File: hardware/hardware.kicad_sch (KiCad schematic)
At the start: 5 parts, among them J1 USB_C_Receptacle_USB2.0_14P, J3 Conn_01x08_Socket, U2 ESP32-S3-WROOM-1

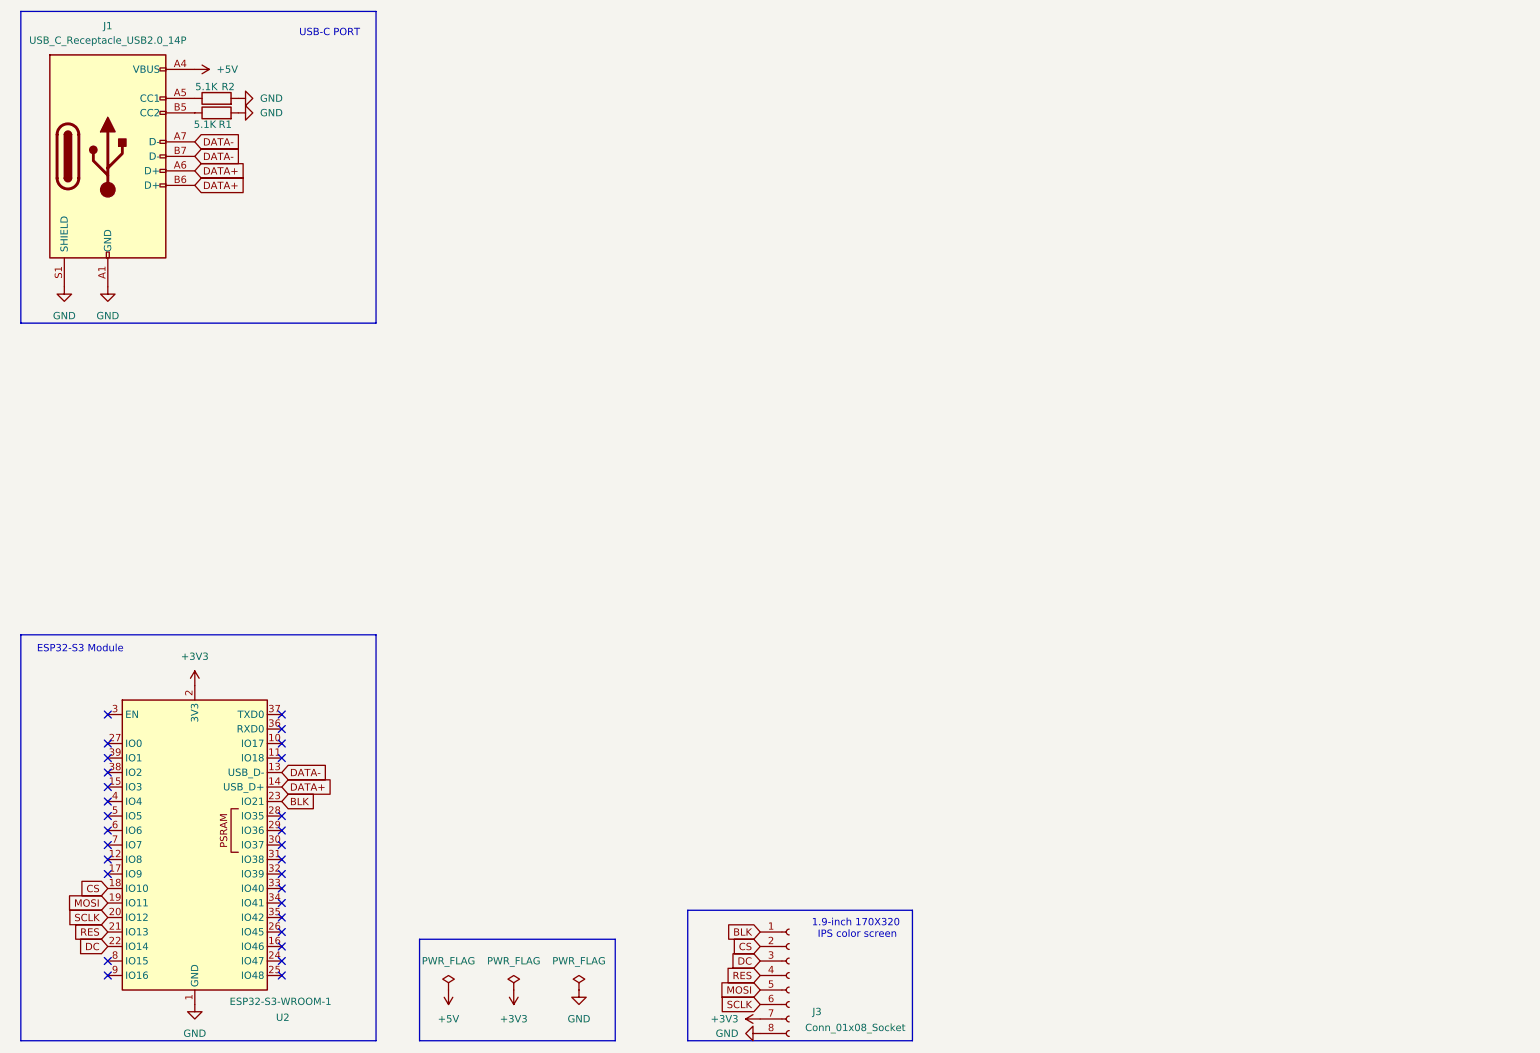
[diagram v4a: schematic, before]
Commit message: Adding AMS117 Voltage divider (NO CAPACITOR)
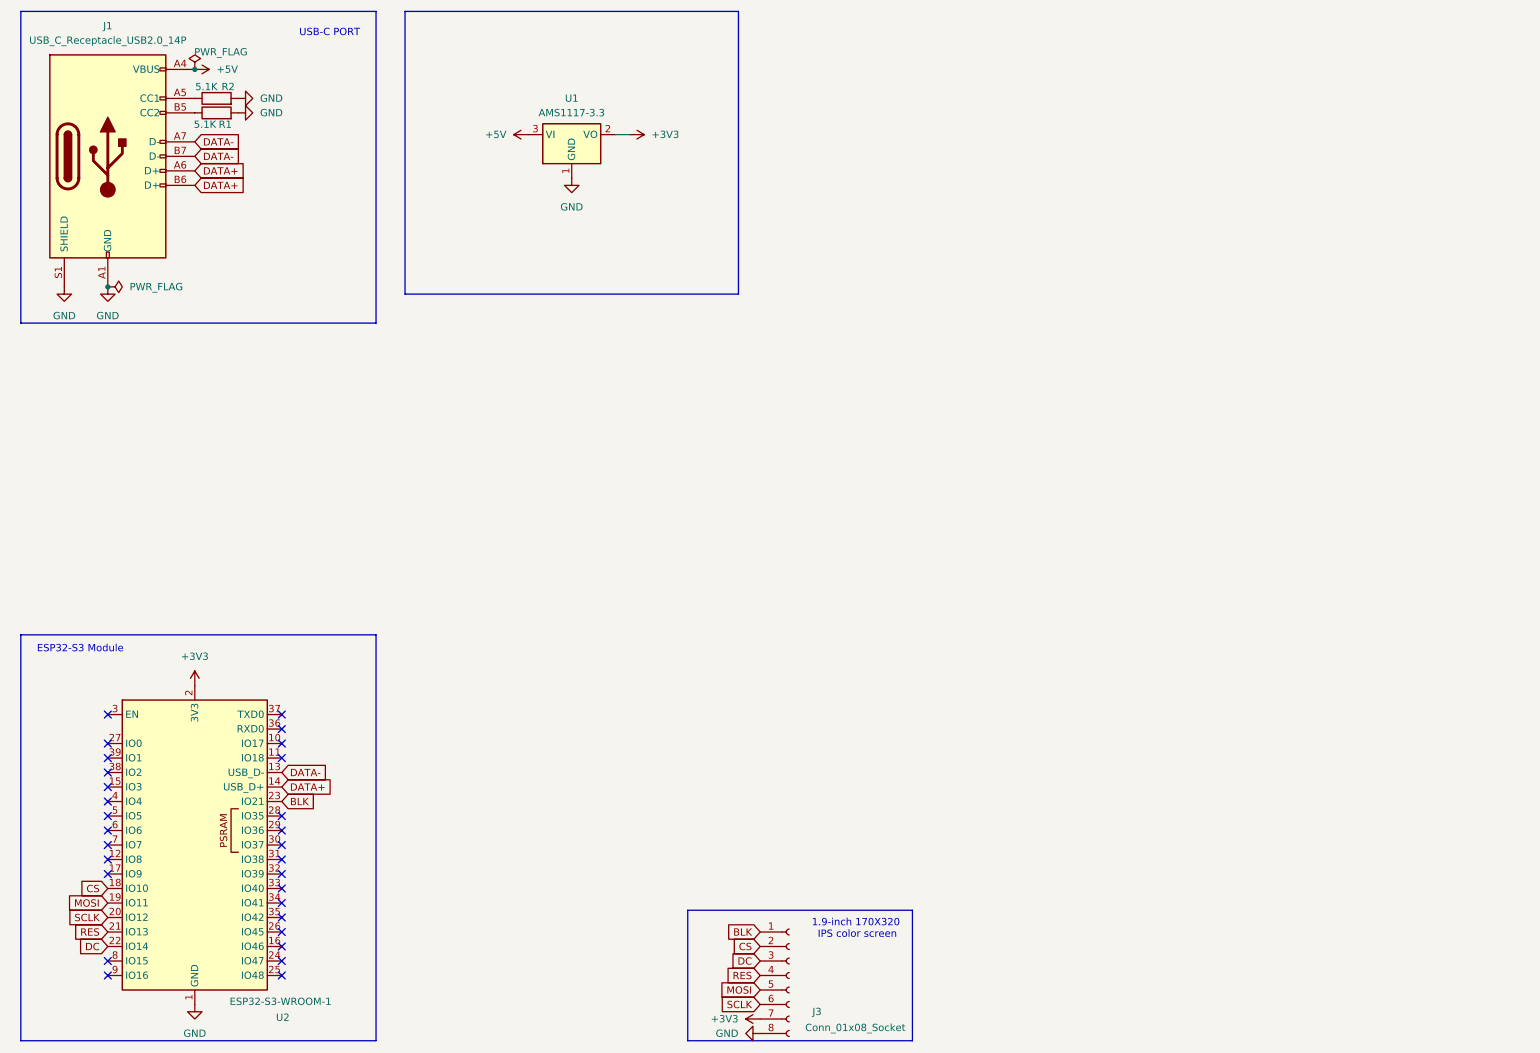
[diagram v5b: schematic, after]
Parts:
- added U1: AMS1117-3.3, Package_TO_SOT_SMD:SOT-223-3_TabPin2, symbol Regulator_Linear:AMS1117-3.3
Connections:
- net +3V3: now also U1.2 (VO)
- net +5V: now also U1.3 (VI)
- net GND: now also U1.1 (GND)

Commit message: Adding DHT sensor pins
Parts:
- added J4: Conn_01x04_Socket, symbol Connector:Conn_01x04_Socket
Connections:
- net +3V3: now also J4.1 (Pin_1)
- net GND: now also J4.4 (Pin_4)
- net DHT11: now reaches U2.9 (IO16)
- net DHT11: now also J4.2 (Pin_2)
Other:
- note added: "DHT SENSOR"
- moved on the sheet: J3

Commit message: Adding soil sensor pins
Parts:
- added J2: Conn_01x04_Socket, symbol Connector:Conn_01x04_Socket
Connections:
- net +3V3: now also J2.1 (Pin_1)
- net GND: now also J2.2 (Pin_2)
- new net AO_SOIL: J2.4 (Pin_4)
- new net DO_SOIL: J2.3 (Pin_3)
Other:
- note added: "SOIL SENSOR"

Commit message: [ERC VERIFIED] Adding soil sensor pin
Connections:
- net AO_SOIL: now also U2.11 (IO18)
- net DO_SOIL: no longer names the net of J2.3 (Pin_3)
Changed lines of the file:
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@@
+	)
+	(no_connect
+		(at 195.58 26.67)
 	)
 	(no_connect
@@
 	(no_connect
 		(at 60.96 182.88)
-	)
-	(no_connect
-		(at 60.96 144.78)
 	)
 	(no_connect
@@
 		)
 	)
-	(global_label "DO_SOIL"
-		(shape input)
-		(at 195.58 26.67 180)
-		(fields_autoplaced yes)
-		(effects
-			(font
-				(size 1.27 1.27)
-			)
-			(justify right)
-		)
-		(property "Intersheetrefs" "${INTERSHEET_REFS}"
-			(at 189.9943 26.67 0)
-			(effects
-				(font
-					(size 1.27 1.27)
-				)
-				(justify right)
-				(hide yes)
-			)
-		)
-	)
 	(global_label "RES"
 		(shape input)
@@
 				(hide yes)
 			)
+		)
+	)
+	(global_label "AO_SOIL"
+		(shape input)
+		(at 60.96 144.78 0)
+		(fields_autoplaced yes)
+		(effects
+			(font
+				(size 1.27 1.27)
+			)
+			(justify left)
+		)
+		(property "Intersheetrefs" "${INTERSHEET_REFS}"
+			(at 71.5048 144.78 0)
+			(effects
+				(font
+					(size 1.27 1.27)
+				)
+				(justify left)
+				(hide yes)
+			)
